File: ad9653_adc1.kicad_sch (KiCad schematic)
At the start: 20 parts, among them J701 142-0701-201, J702 142-0701-201, J703 142-0701-201, J704 142-0701-201, U701 AD9653BCPZ-125

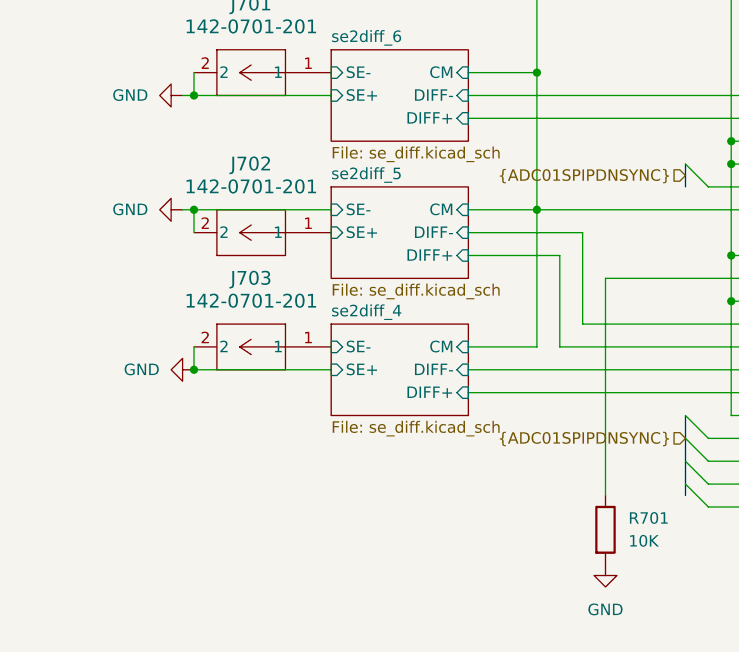
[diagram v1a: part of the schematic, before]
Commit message: Added -3.3V supply, buffer amplifier, and single-to-differential op-amp circuit
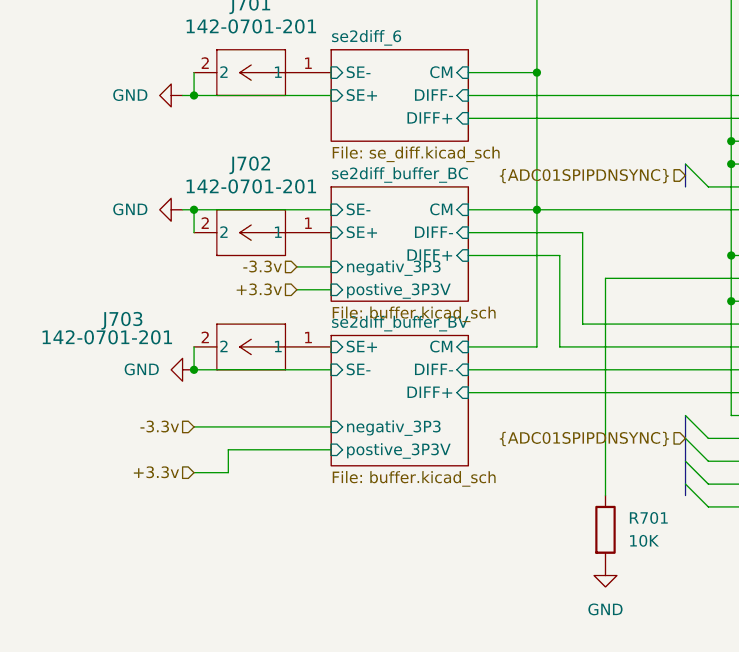
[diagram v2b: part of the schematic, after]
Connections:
- net se2diff_buffer_BV/CM renamed se2diff_6/CM
- net se2diff_buffer_BV/SE- renamed se2diff_buffer_BV/SE+
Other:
- sheet se2diff_4 renamed se2diff_buffer_BV
- sheet se2diff_5 renamed se2diff_buffer_BC
- sheet se2diff_buffer_BC: file se_diff.kicad_sch -> buffer.kicad_sch
- sheet se2diff_buffer_BC ports: added negativ_3P3, postive_3P3V; removed none
- sheet se2diff_buffer_BV: file se_diff.kicad_sch -> buffer.kicad_sch
- sheet se2diff_buffer_BV ports: added negativ_3P3, postive_3P3V; removed none
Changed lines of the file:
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@@
 	(wire
 		(pts
+			(xy 41.91 109.22) (xy 45.72 109.22)
+		)
+		(stroke
+			(width 0)
+			(type default)
+		)
+	)
+	(wire
+		(pts
 			(xy 87.63 135.89) (xy 128.27 135.89)
 		)
@@
 	(wire
 		(pts
+			(xy 41.91 111.76) (xy 45.72 111.76)
+		)
+		(stroke
+			(width 0)
+			(type default)
+		)
+	)
+	(wire
+		(pts
 			(xy 199.39 135.89) (xy 231.14 135.89)
 		)
@@
 	(wire
 		(pts
+			(xy 34.29 129.54) (xy 34.29 132.08)
+		)
+		(stroke
+			(width 0)
+			(type default)
+		)
+	)
+	(wire
+		(pts
 			(xy 199.39 110.49) (xy 231.14 110.49)
 		)
@@
 	(wire
 		(pts
+			(xy 45.72 129.54) (xy 34.29 129.54)
+		)
+		(stroke
+			(width 0)
+			(type default)
+		)
+	)
+	(wire
+		(pts
 			(xy 200.66 95.25) (xy 200.66 92.71)
 		)
@@
 	(wire
 		(pts
+			(xy 30.48 127) (xy 45.72 127)
+		)
+		(stroke
+			(width 0)
+			(type default)
+		)
+	)
+	(wire
+		(pts
 			(xy 68.58 69.85) (xy 207.01 69.85)
 		)
@@
 	(wire
 		(pts
+			(xy 34.29 132.08) (xy 30.48 132.08)
+		)
+		(stroke
+			(width 0)
+			(type default)
+		)
+	)
+	(wire
+		(pts
 			(xy 48.26 60.96) (xy 54.61 60.96)
 		)
@@
 		)
 	)
+	(hierarchical_label "-3.3v"
+		(shape input)
+		(at 30.48 127 180)
+		(fields_autoplaced yes)
+		(effects
+			(font
+				(size 1.27 1.27)
+			)
+			(justify right)
+		)
+	)
+	(hierarchical_label "+3.3v"
+		(shape input)
+		(at 41.91 111.76 180)
+		(fields_autoplaced yes)
+		(effects
+			(font
+				(size 1.27 1.27)
+			)
+			(justify right)
+		)
+	)
 	(hierarchical_label "ADC"
 		(shape input)
@@
 		)
 	)
+	(hierarchical_label "-3.3v"
+		(shape input)
+		(at 41.91 109.22 180)
+		(fields_autoplaced yes)
+		(effects
+			(font
+				(size 1.27 1.27)
+			)
+			(justify right)
+		)
+	)
 	(hierarchical_label "VSS1P8V"
 		(shape input)
@@
 		)
 	)
+	(hierarchical_label "+3.3v"
+		(shape input)
+		(at 30.48 132.08 180)
+		(fields_autoplaced yes)
+		(effects
+			(font
+				(size 1.27 1.27)
+			)
+			(justify right)
+		)
+	)
 	(hierarchical_label "{ADC01SPIPDNSYNC}"
 		(shape input)
@@
 		(on_board yes)
 		(dnp no)
-		(fields_autoplaced yes)
 		(property "Reference" "J703"
-			(at 36.83 110.49 0)
+			(at 22.606 115.062 0)
 			(effects
 				(font
@@
 		)
 		(property "Value" "142-0701-201"
-			(at 36.83 113.03 0)
+			(at 20.828 117.094 0)
 			(effects
 				(font
@@
 	)
 	(sheet
-		(at 45.72 115.57)
-		(size 15.24 10.16)
+		(at 45.72 116.84)
+		(size 15.24 14.478)
 		(fields_autoplaced yes)
 		(stroke
@@
 			(color 0 0 0 0.0000)
 		)
-		(property "Sheetname" "se2diff_4"
-			(at 45.72 114.8584 0)
+		(property "Sheetname" "se2diff_buffer_BV"
+			(at 45.72 116.1284 0)
 			(effects
 				(font
@@
 			)
 		)
-		(property "Sheetfile" "se_diff.kicad_sch"
-			(at 45.72 126.3146 0)
+		(property "Sheetfile" "buffer.kicad_sch"
+			(at 45.72 131.9026 0)
 			(effects
 				(font
@@
 		)
 		(pin "SE-" input
-			(at 45.72 118.11 180)
+			(at 45.72 120.65 180)
 			(effects
 				(font
@@
 		)
 		(pin "SE+" input
-			(at 45.72 120.65 180)
+			(at 45.72 118.11 180)
+			(effects
+				(font
+					(size 1.27 1.27)
+				)
+				(justify left)
+			)
+		)
+		(pin "negativ_3P3" input
+			(at 45.72 127 180)
+			(effects
+				(font
+					(size 1.27 1.27)
+				)
+				(justify left)
+			)
+		)
+		(pin "postive_3P3V" input
+			(at 45.72 129.54 180)
 			(effects
 				(font
@@
 	(sheet
 		(at 45.72 100.33)
-		(size 15.24 10.16)
+		(size 15.24 12.7)
 		(fields_autoplaced yes)
 		(stroke
@@
 			(color 0 0 0 0.0000)
 		)
-		(property "Sheetname" "se2diff_5"
+		(property "Sheetname" "se2diff_buffer_BC"
 			(at 45.72 99.6184 0)
 			(effects
@@
 			)
 		)
-		(property "Sheetfile" "se_diff.kicad_sch"
-			(at 45.72 111.0746 0)
+		(property "Sheetfile" "buffer.kicad_sch"
+			(at 45.72 113.6146 0)
 			(effects
 				(font
@@
 			(effects
 				(font
+					(size 1.27 1.27)
+				)
+				(justify left)
+			)
+		)
+		(pin "negativ_3P3" input
+			(at 45.72 109.22 180)
+			(effects
+				(font
+					(size 1.27 1.27)
+				)
+				(justify left)
+			)
+		)
+		(pin "postive_3P3V" input
+			(at 45.72 111.76 180)
+			(effects
+				(font
